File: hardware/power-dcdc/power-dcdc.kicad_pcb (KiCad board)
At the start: 2 copper layers, 110 x 70 mm, 85 parts, among them J1 SOLAR_IN, J2 DCDC-MEASURES, J3 DCDC-PWM, J4 BATT2, J5 BATT1, Q1 SIR186LDP, Q2 SIR186LDP, Q3 SI7149ADP, Q4 SI7149ADP, Q5 SI7149ADP, Q6 SI7149ADP, Q7 BSS123, Q8 BSS123, U1 LP4951C, U2 NCP5901B, U3 PAC1953-1, U4 DGD0215, U5 DGD0215

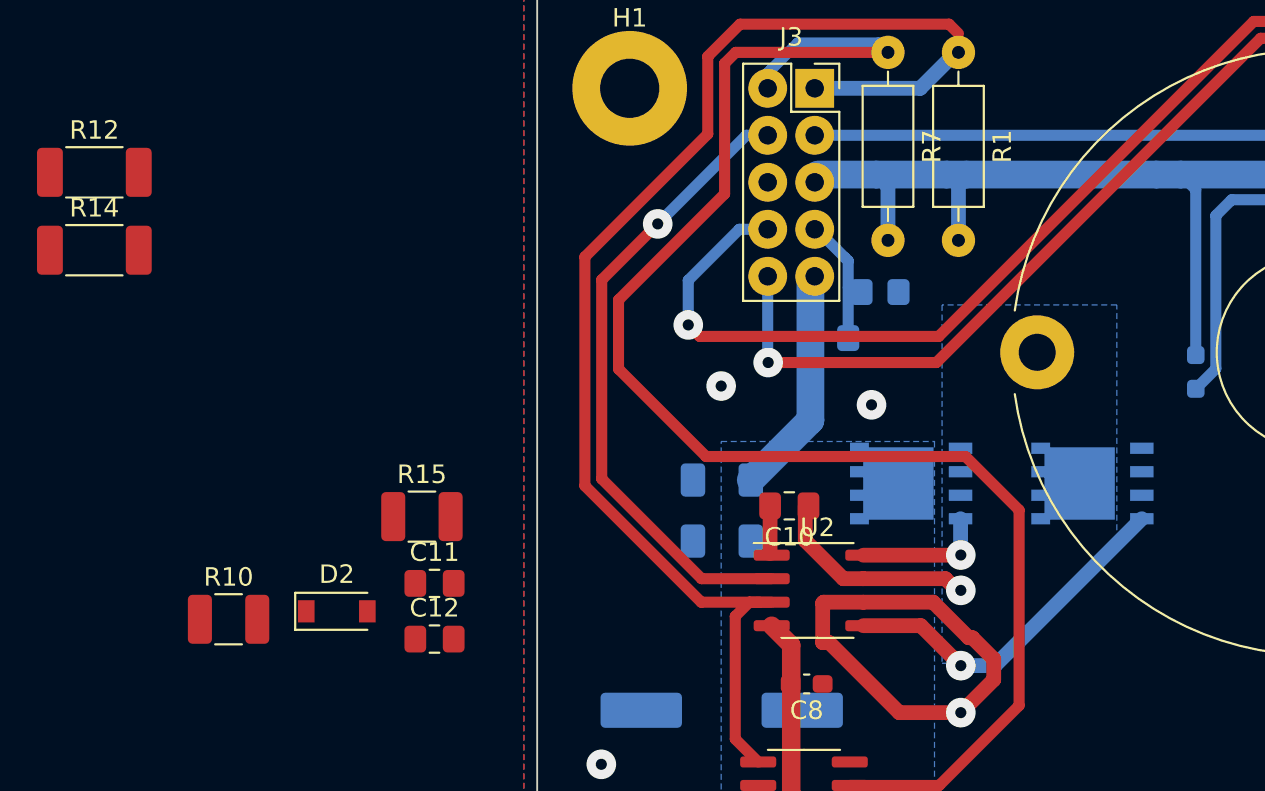
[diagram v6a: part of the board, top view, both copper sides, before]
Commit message: dcdc PCB: work in progress on switch node. Needs to move input capacitor to the right side of the solar power track; current loop through mosfets is way too long as it is !
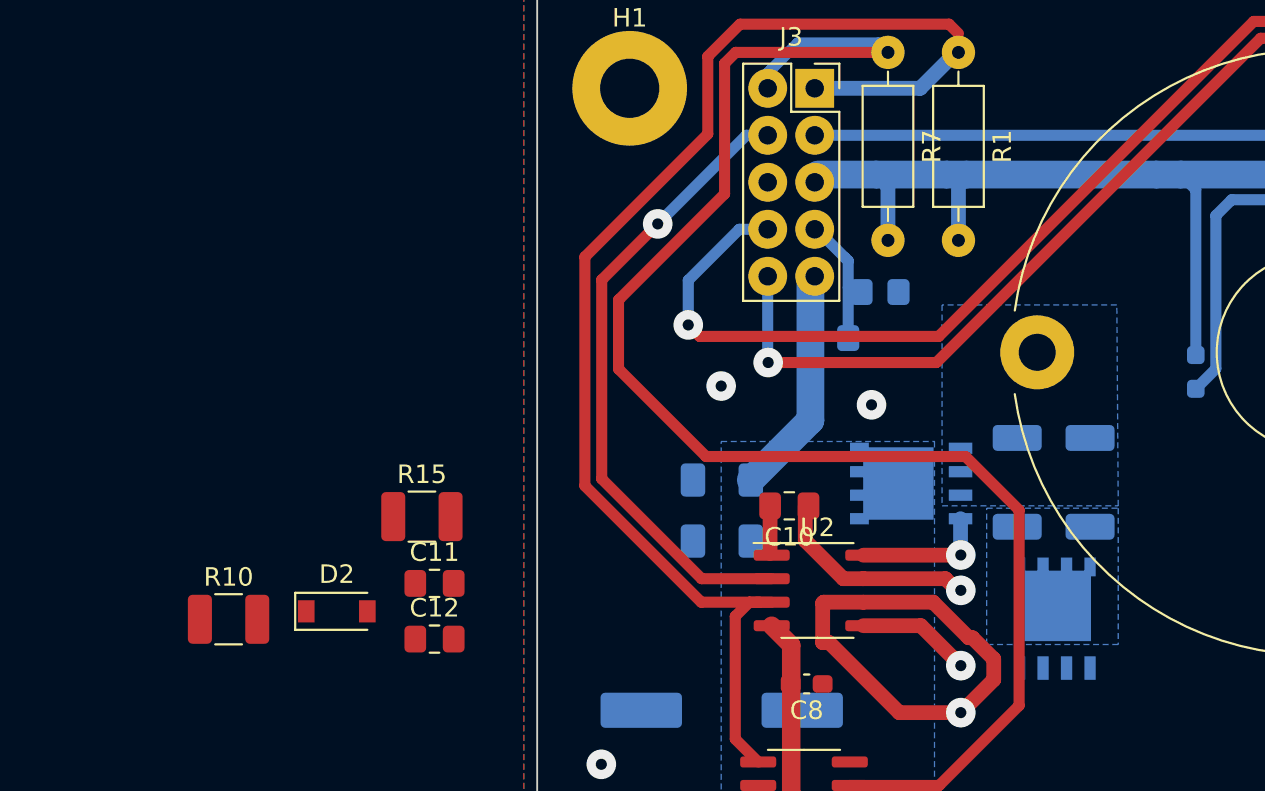
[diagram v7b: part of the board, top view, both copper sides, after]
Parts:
- R12, R14: moved to B.Cu
- moved R12 56.4 mm to (79.9, 106.3), turned to 90 degrees
- moved R14 51.4 mm to (75.9, 106.3), turned to 90 degrees
- moved Q2 7.58 mm to (78.0, 113.7), turned to 90 degrees
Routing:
- net Net-(Q2-Pad4): track 19.2 -> 6.17 mm
- added copper zone on B.Cu, net Net-(Q2-Pad5)

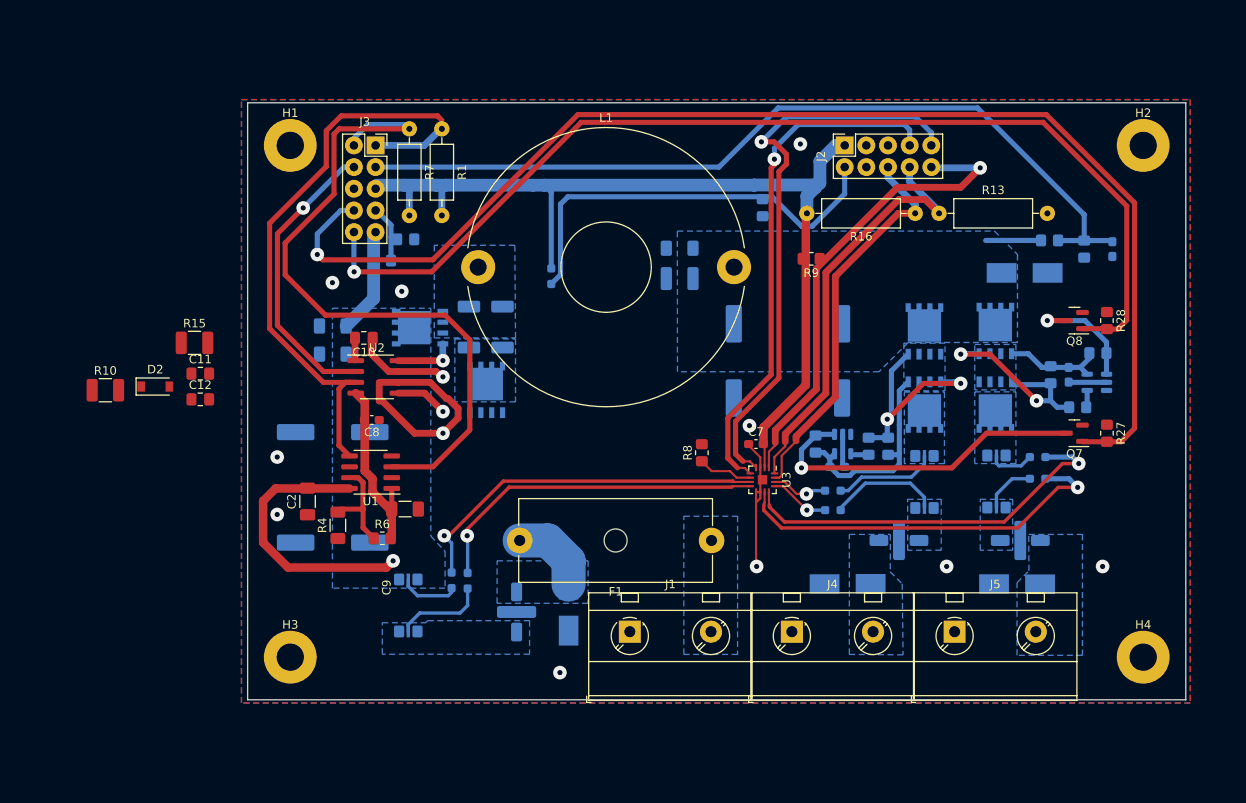
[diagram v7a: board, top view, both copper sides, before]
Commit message: Finish re-implementing the SW node. Enlarge ground vias.
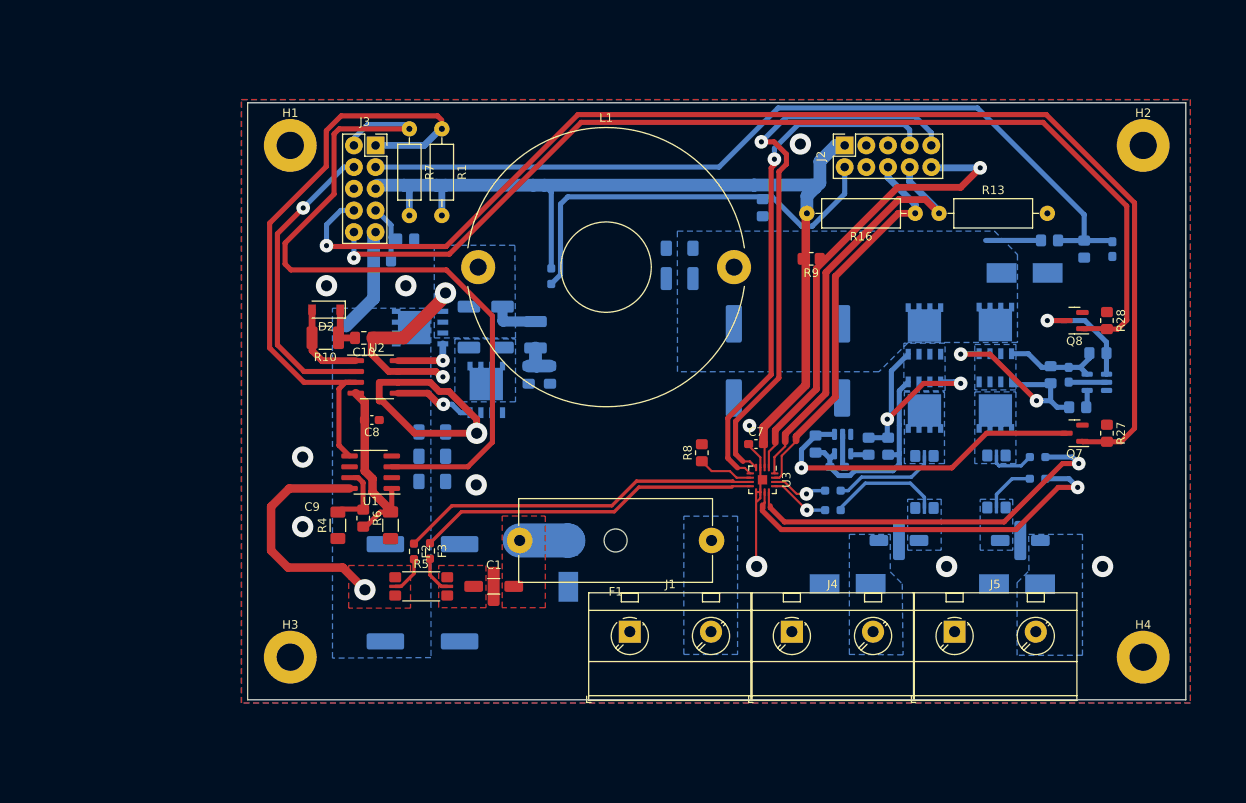
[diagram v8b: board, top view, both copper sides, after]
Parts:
- C1, F2, F3, R5: moved to F.Cu
- C11, C12, C2, R15: moved to B.Cu
- moved C12 41.1 mm to (85.5, 111.9), turned to -90 degrees
- moved R15 40.0 mm to (83.8, 107.2), turned to -90 degrees
- moved C11 38.5 mm to (83.0, 111.9), turned to -90 degrees
- moved R10 26.5 mm to (59.1, 107.5), turned to 180 degrees
- moved D2 22.0 mm to (59.2, 104.2), turned to 180 degrees
- moved C3 21.6 mm to (71.7, 124.4), turned to 0 degrees
- moved C6 16.8 mm to (70.5, 131.8), turned to 0 degrees
- moved C2 16.7 mm to (71.7, 118.6), turned to 180 degrees
- moved C4 16.7 mm to (71.7, 121.5), turned to 0 degrees
- moved C5 15.6 mm to (70.5, 143.2), turned to 0 degrees
- moved F3 5.63 mm to (71.4, 132.6)
- moved F2 5.57 mm to (69.5, 132.6)
- moved D1 5.14 mm to (87.6, 134.1)
- moved C1 4.03 mm to (78.8, 136.7), turned to 0 degrees
- moved R6 3.25 mm to (63.5, 128.7), turned to -90 degrees
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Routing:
- net Net-(C10-Pad1): track 11.4 -> 27.9 mm, vias 1 -> 2
- net Net-(D2-Pad2): track 2.58 -> 10.4 mm
- net /PWM_OFF: track 83.1 -> 90.1 mm
- net Net-(F3-Pad2): track 10.7 -> 4.48 mm
- net Net-(C10-Pad2): track 0.00 -> 5.33 mm
- net Net-(C11-Pad1): track 0.00 -> 4.67 mm
- net GND: track 50.0 -> 54.6 mm
- net /SOLAR_PWR: track 44.8 -> 40.6 mm
- net Net-(R4-Pad2): track 10.8 -> 6.89 mm
- net Net-(C1-Pad3): track 9.50 -> 5.72 mm
- net BATT2_ON: track 148.5 -> 145.0 mm
- net Net-(Q2-Pad4): track 6.17 -> 9.40 mm
- net Net-(F2-Pad2): track 6.99 -> 4.51 mm
- net BATT1_ON: track 125.6 -> 123.4 mm
- net /PWM: track 34.4 -> 35.7 mm
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- added copper zone on F.Cu, net /SOLAR+
- added copper zone on F.Cu, net /SOLAR_PWR
- added copper zone on F.Cu, net Net-(C1-Pad3)
- removed copper zone on B.Cu, net /SOLAR+
- removed copper zone on B.Cu, net Net-(C1-Pad3)
